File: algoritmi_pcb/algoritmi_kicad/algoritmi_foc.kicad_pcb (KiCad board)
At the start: 2 copper layers, 81.2 x 81.2 mm, 43 parts, among them IC2 AP2114HA-3.3TRG1, J2 53261-0371, J3 SMM-115-02-S-D-LC-K-TR, U1 TMC6300-LA-T, U2 MT6701CT-STD

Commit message: New updates
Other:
- outline, holes or cut-outs redrawn

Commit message: adding the presure sensitive click pcb
I forgot to put it in the right position :)
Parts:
- added C11: 0.1uF, Capacitor_SMD:C_0603_1608Metric, F.Cu at (62.0, 90.8)
- added C12: 10uF, Capacitor_SMD:C_0805_2012Metric, F.Cu at (76.4, 86.4)
- added C13: 0.1uF, Capacitor_SMD:C_0603_1608Metric, F.Cu at (78.4, 86.4)
- added C14: 0.1uF, Capacitor_SMD:C_0603_1608Metric, F.Cu at (66.6, 92.4)
- added C15: 0.1uF, Capacitor_SMD:C_0603_1608Metric, F.Cu at (62.2, 92.4)
- added C6: 10uF, Capacitor_SMD:C_0805_2012Metric, F.Cu at (62.0, 88.8)
- added L1: 3.3uH, Inductor_SMD:L_0805_2012Metric, F.Cu at (62.0, 86.8)
- added Q1: MMBT4403, Package_TO_SOT_SMD:SOT-23, F.Cu at (60.6, 80.0)
- added R15: 330, Resistor_SMD:R_2512_6332Metric, B.Cu at (83.8, 85.2)
- added R16: 330, Resistor_SMD:R_2512_6332Metric, F.Cu at (79.2, 95.8)
- added R17: 330, Resistor_SMD:R_2512_6332Metric, F.Cu at (87.0, 95.6)
- added R18: 330, Resistor_SMD:R_2512_6332Metric, F.Cu at (79.0, 91.8)
- added R19: 100, Resistor_SMD:R_0603_1608Metric, F.Cu at (62.2, 94.2)
- added R20: 100, Resistor_SMD:R_0603_1608Metric, F.Cu at (62.2, 95.8)
- added R21: 10k, Resistor_SMD:R_0603_1608Metric, F.Cu at (65.6, 88.0)
- added R22: 8.2k, Resistor_SMD:R_0603_1608Metric, F.Cu at (77.4, 89.0)
- added U3: HX711, Package_SO:SOIC-16_3.9x9.9mm_P1.27mm, F.Cu at (71.1, 88.6)
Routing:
- net /STRAIN_E+: track 0.00 -> 55.4 mm, vias 0 -> 1
- net GNDA: track 0.00 -> 43.1 mm, vias 0 -> 3
- net /STRAIN_S-: track 0.00 -> 33.8 mm
- net /STRAIN_S+: track 0.00 -> 33.2 mm, vias 0 -> 1
- net +3V3: track 0.00 -> 20.3 mm
- net Net-(Q1-C): track 0.00 -> 20.2 mm
- net Net-(U3-VFB): track 0.00 -> 12.2 mm
- net Net-(Q1-B): track 0.00 -> 8.98 mm
- net Net-(U3-INA-): track 0.00 -> 6.79 mm
- net Net-(U3-INA+): track 0.00 -> 6.75 mm
- net Net-(U3-VBG): track 0.00 -> 6.44 mm
- net GND: vias 21 -> 22

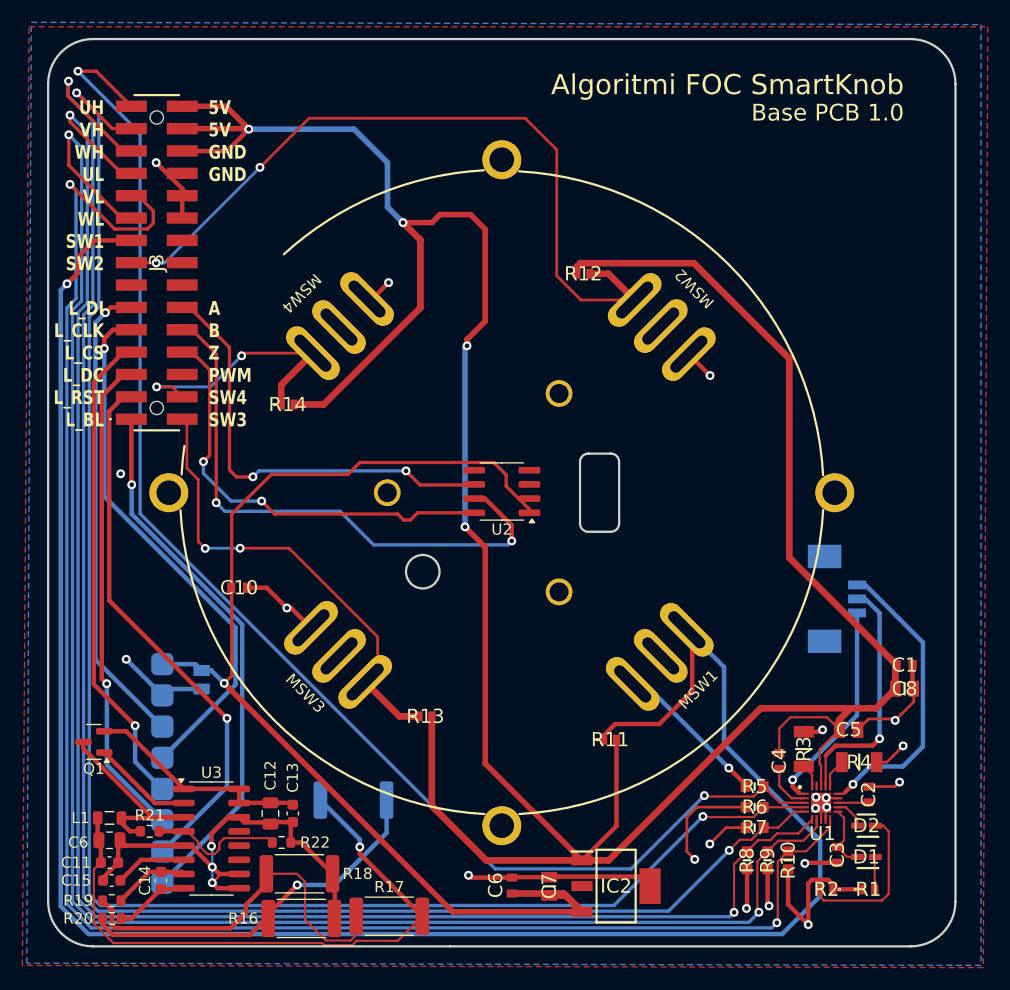
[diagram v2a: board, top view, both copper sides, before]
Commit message: updated positioning of presure sensors
NOTE: the GND on the presure sensor circuit is not connected to the GND of the whole circuit.
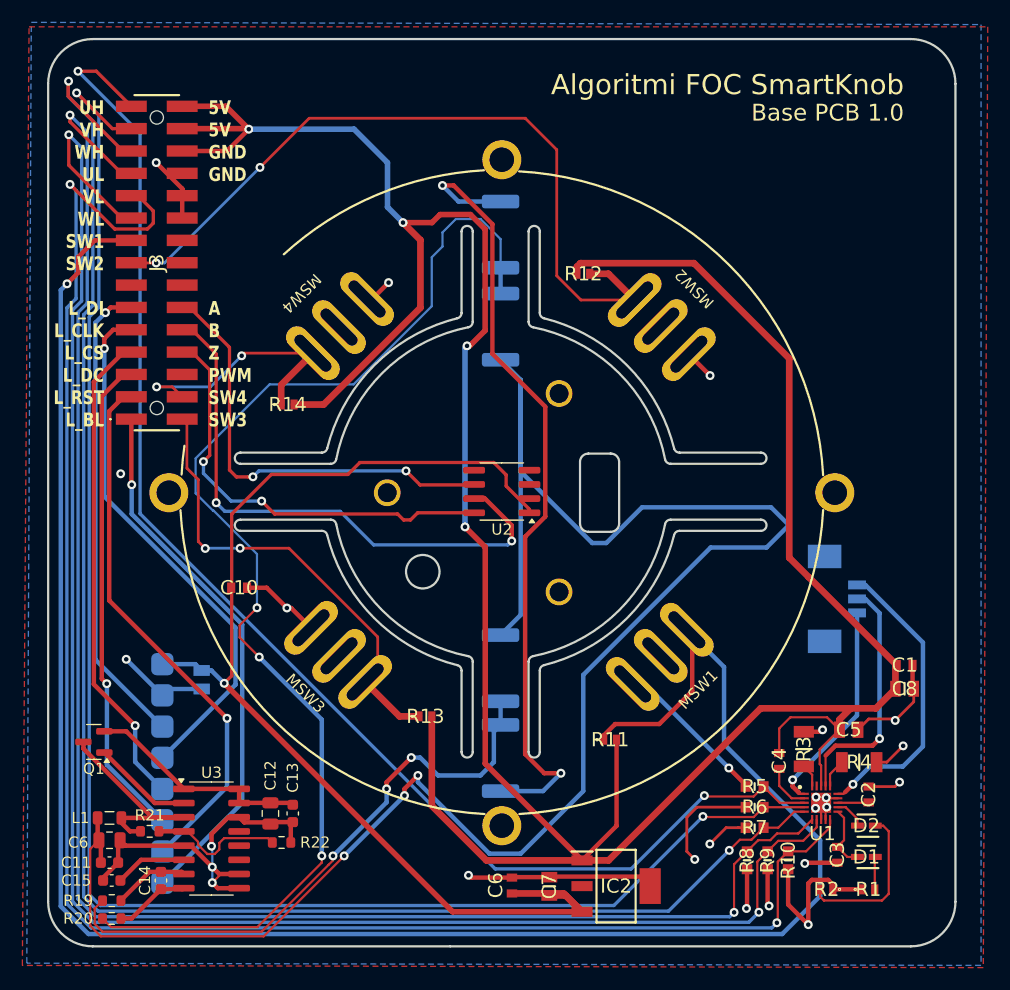
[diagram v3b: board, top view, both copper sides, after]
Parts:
- R16, R17, R18: moved to B.Cu
- moved R16 63.7 mm to (97.0, 34.6), turned to 90 degrees
- moved R15 44.4 mm to (97.0, 42.8), turned to 90 degrees
- moved R17 24.3 mm to (97.0, 73.4), turned to 90 degrees
- moved R18 20.8 mm to (97.0, 81.4), turned to 90 degrees
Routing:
- net /STRAIN_E+: track 55.4 -> 166.0 mm, vias 1 -> 3
- net /STRAIN_S+: track 33.2 -> 111.9 mm, vias 1 -> 3
- net GNDA: track 43.1 -> 106.1 mm, vias 3 -> 5
- net /STRAIN_S-: track 33.8 -> 53.0 mm, vias 0 -> 3
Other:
- outline, holes or cut-outs redrawn
